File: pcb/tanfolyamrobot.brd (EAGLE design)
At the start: 81.3 x 58.7 mm, 85 parts, among them IC1 STM32F10XRXT6, IC2 7805, IC4 FT232RL, IC5 LD117AS33TR, M1 DRV8833, Q1 AO4407A, Q2 BSS123, Q3 BSS123, Q4 BSS123, X1 CSTCE08M, X2 PWR

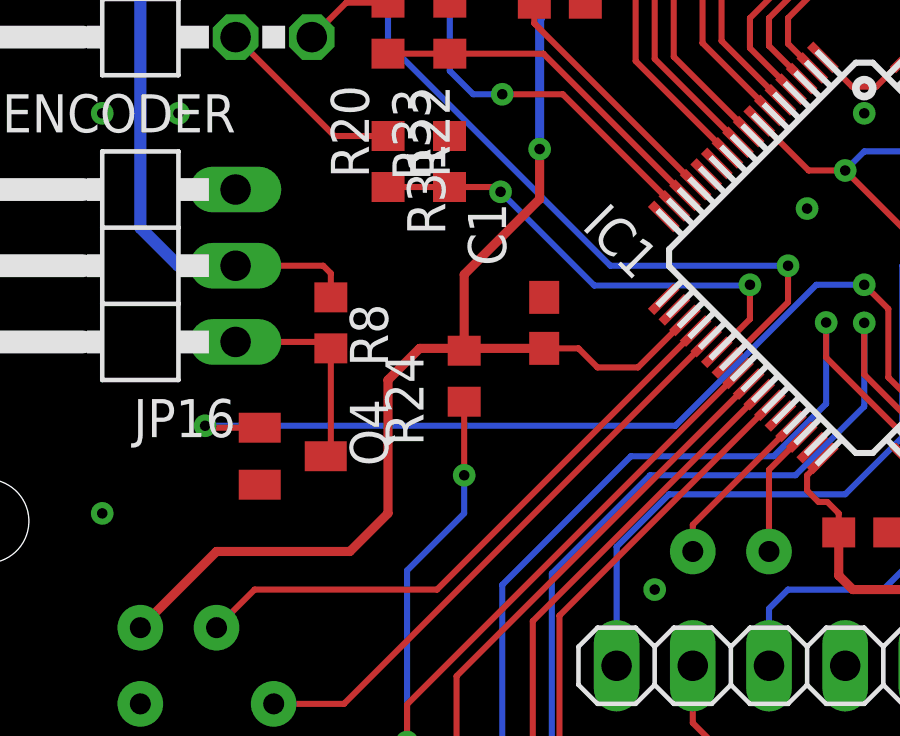
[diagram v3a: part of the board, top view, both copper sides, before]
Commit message: removed motor_faultn pullup (#1)
it can be pulled up in stm
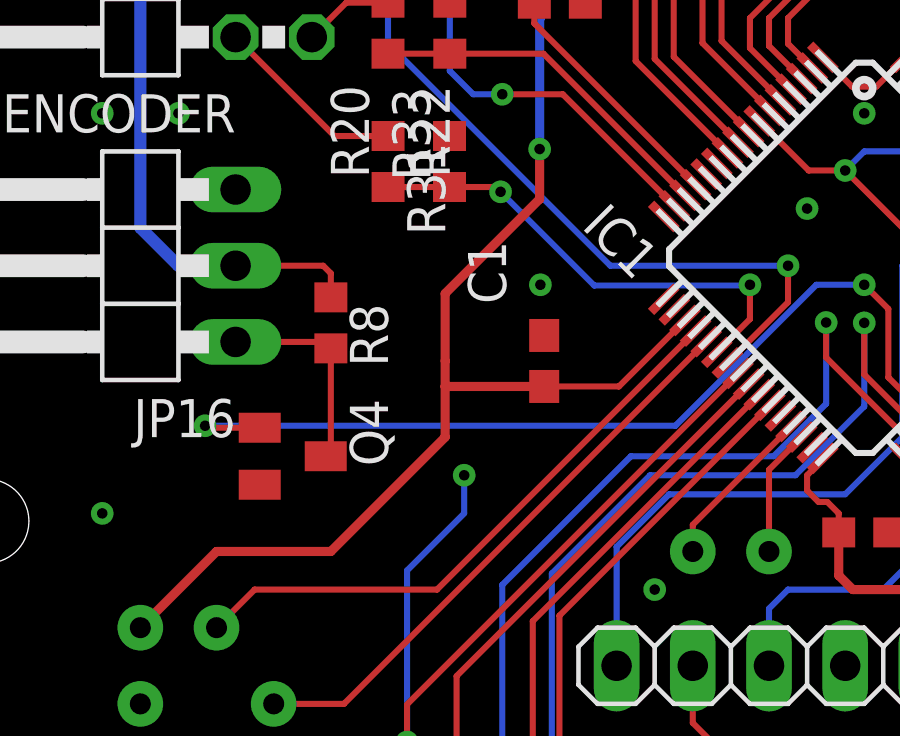
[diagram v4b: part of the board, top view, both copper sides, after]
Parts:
- removed R24: 4K7, rcl:R0603
- moved C1 1.27 mm to (21.7, 29.8)
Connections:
- net +3V3: no longer R24.1
- net MOTOR_FAULTN: no longer R24.2
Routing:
- net MOTOR_FAULTN: track 46.3 -> 43.8 mm
- net +3V3: track 241.4 -> 240.7 mm
- net GND: vias 53 -> 54
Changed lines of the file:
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@@
 <grid distance="25" unitdist="mil" unit="mil" style="dots" multiple="1" display="yes" altdistance="6.125" altunitdist="mil" altunit="mil"/>
 <layers>
-<layer number="1" name="Top" color="4" fill="1" visible="no" active="yes"/>
+<layer number="1" name="Top" color="4" fill="1" visible="yes" active="yes"/>
 <layer number="2" name="Route2" color="16" fill="1" visible="no" active="no"/>
 <layer number="3" name="Route3" color="17" fill="1" visible="no" active="no"/>
@@
 <layer number="19" name="Unrouted" color="6" fill="1" visible="yes" active="yes"/>
 <layer number="20" name="Dimension" color="24" fill="1" visible="yes" active="yes"/>
-<layer number="21" name="tPlace" color="7" fill="1" visible="no" active="yes"/>
-<layer number="22" name="bPlace" color="7" fill="1" visible="no" active="yes"/>
-<layer number="23" name="tOrigins" color="13" fill="1" visible="no" active="yes"/>
-<layer number="24" name="bOrigins" color="13" fill="1" visible="no" active="yes"/>
+<layer number="21" name="tPlace" color="7" fill="1" visible="yes" active="yes"/>
+<layer number="22" name="bPlace" color="7" fill="1" visible="yes" active="yes"/>
+<layer number="23" name="tOrigins" color="13" fill="1" visible="yes" active="yes"/>
+<layer number="24" name="bOrigins" color="13" fill="1" visible="yes" active="yes"/>
 <layer number="25" name="tNames" color="7" fill="1" visible="no" active="yes"/>
 <layer number="26" name="bNames" color="7" fill="1" visible="no" active="yes"/>
@@
 <layer number="37" name="tTest" color="7" fill="1" visible="no" active="yes"/>
 <layer number="38" name="bTest" color="7" fill="1" visible="no" active="yes"/>
-<layer number="39" name="tKeepout" color="4" fill="11" visible="no" active="yes"/>
-<layer number="40" name="bKeepout" color="1" fill="11" visible="no" active="yes"/>
-<layer number="41" name="tRestrict" color="4" fill="10" visible="no" active="yes"/>
-<layer number="42" name="bRestrict" color="1" fill="10" visible="no" active="yes"/>
+<layer number="39" name="tKeepout" color="4" fill="11" visible="yes" active="yes"/>
+<layer number="40" name="bKeepout" color="1" fill="11" visible="yes" active="yes"/>
+<layer number="41" name="tRestrict" color="4" fill="10" visible="yes" active="yes"/>
+<layer number="42" name="bRestrict" color="1" fill="10" visible="yes" active="yes"/>
 <layer number="43" name="vRestrict" color="2" fill="10" visible="no" active="yes"/>
 <layer number="44" name="Drills" color="7" fill="1" visible="no" active="yes"/>
@@
 <layer number="49" name="Reference" color="7" fill="1" visible="no" active="yes"/>
 <layer number="50" name="dxf" color="7" fill="1" visible="no" active="no"/>
-<layer number="51" name="tDocu" color="7" fill="1" visible="no" active="yes"/>
-<layer number="52" name="bDocu" color="7" fill="1" visible="no" active="yes"/>
+<layer number="51" name="tDocu" color="7" fill="1" visible="yes" active="yes"/>
+<layer number="52" name="bDocu" color="7" fill="1" visible="yes" active="yes"/>
 <layer number="53" name="tGND_GNDA" color="7" fill="9" visible="no" active="no"/>
 <layer number="54" name="bGND_GNDA" color="1" fill="9" visible="no" active="no"/>
@@
 <attribute name="VALUE" x="28.259665625" y="34.90505625" size="1.778" layer="27" rot="R315"/>
 </element>
-<element name="C1" library="rcl" library_urn="urn:adsk.eagle:library:334" package="C0603" package3d_urn="urn:adsk.eagle:package:23616/2" value="100n" x="21.717" y="31.115" smashed="yes" rot="R90">
-<attribute name="NAME" x="20.447" y="33.02" size="1.27" layer="25" rot="R90"/>
-<attribute name="POPULARITY" value="73" x="21.717" y="31.115" size="1.778" layer="27" rot="R90" display="off"/>
-<attribute name="SPICEPREFIX" value="C" x="21.717" y="31.115" size="1.778" layer="27" rot="R90" display="off"/>
-<attribute name="VALUE" x="23.622" y="30.48" size="1.27" layer="27" rot="R90"/>
+<element name="C1" library="rcl" library_urn="urn:adsk.eagle:library:334" package="C0603" package3d_urn="urn:adsk.eagle:package:23616/2" value="100n" x="21.717" y="29.845" smashed="yes" rot="R90">
+<attribute name="NAME" x="20.447" y="31.75" size="1.27" layer="25" rot="R90"/>
+<attribute name="POPULARITY" value="73" x="21.717" y="29.845" size="1.778" layer="27" rot="R90" display="off"/>
+<attribute name="SPICEPREFIX" value="C" x="21.717" y="29.845" size="1.778" layer="27" rot="R90" display="off"/>
+<attribute name="VALUE" x="23.622" y="29.21" size="1.27" layer="27" rot="R90"/>
 </element>
 <element name="C2" library="rcl" library_urn="urn:adsk.eagle:library:334" package="C0603" package3d_urn="urn:adsk.eagle:package:23616/2" value="100n" x="32.385" y="24.13" smashed="yes">
@@
 <attribute name="SPICEPREFIX" value="R" x="18.570575" y="49.82845" size="1.778" layer="27" rot="R90" display="off"/>
 <attribute name="VALUE" x="20.475575" y="49.19345" size="1.27" layer="27" rot="R90"/>
-</element>
-<element name="R24" library="rcl" library_urn="urn:adsk.eagle:library:334" package="R0603" package3d_urn="urn:adsk.eagle:package:23555/3" value="4K7" x="19.05" y="29.337" smashed="yes" rot="R270">
-<attribute name="NAME" x="16.423534375" y="30.10339375" size="1.27" layer="25" rot="R270"/>
-<attribute name="POPULARITY" value="70" x="19.05" y="29.337" size="1.778" layer="27" rot="R270" display="off"/>
-<attribute name="SPICEPREFIX" value="R" x="19.05" y="29.337" size="1.778" layer="27" rot="R270" display="off"/>
-<attribute name="VALUE" x="17.145" y="29.972" size="1.27" layer="27" rot="R270"/>
 </element>
 <element name="R25" library="rcl" library_urn="urn:adsk.eagle:library:334" package="R0603" package3d_urn="urn:adsk.eagle:package:23555/3" value="4K7" x="18.796" y="12.065" smashed="yes" rot="R90">
@@
 <contactref element="R34" pad="2"/>
 <contactref element="R33" pad="2"/>
+<via x="21.59" y="32.385" extent="1-16" drill="0.35"/>
 </signal>
 <signal name="+3V3">
@@
 <wire x1="31.006140625" y1="39.96518125" x2="31.982321875" y2="38.989" width="0.2032" layer="1"/>
 <wire x1="32.787675" y1="38.989" x2="33.76385625" y2="39.96518125" width="0.2032" layer="1"/>
-<wire x1="26.409946875" y1="31.197059375" x2="24.8428875" y2="29.63" width="0.2032" layer="1"/>
-<wire x1="24.8428875" y1="29.63" x2="23.495" y2="29.63" width="0.2032" layer="1"/>
-<wire x1="21.717" y1="30.265" x2="22.86" y2="30.265" width="0.2032" layer="1"/>
-<wire x1="23.495" y1="29.63" x2="22.86" y2="30.265" width="0.2032" layer="1"/>
-<contactref element="R24" pad="1"/>
+<wire x1="26.409946875" y1="31.197059375" x2="24.2078875" y2="28.995" width="0.2032" layer="1"/>
+<wire x1="21.717" y1="28.995" x2="24.2078875" y2="28.995" width="0.2032" layer="1"/>
 <contactref element="R29" pad="1"/>
 <via x="52.705" y="43.18" extent="1-16" drill="0.35"/>
@@
 <wire x1="21.5646" y1="41.2496" x2="21.5646" y2="36.909375" width="0.3048" layer="16"/>
 <wire x1="8.255" y1="20.955" x2="10.795" y2="23.495" width="0.3048" layer="1"/>
-<wire x1="15.24" y1="23.495" x2="16.51" y2="24.765" width="0.3048" layer="1"/>
-<wire x1="10.795" y1="23.495" x2="15.24" y2="23.495" width="0.3048" layer="1"/>
-<wire x1="16.51" y1="29.21" x2="17.565" y2="30.265" width="0.3048" layer="1"/>
-<wire x1="16.51" y1="29.21" x2="16.51" y2="24.765" width="0.3048" layer="1"/>
-<wire x1="21.717" y1="30.265" x2="19.05" y2="30.265" width="0.3048" layer="1"/>
-<wire x1="19.05" y1="30.265" x2="19.05" y2="30.187" width="0.3048" layer="1"/>
-<wire x1="17.565" y1="30.265" x2="19.05" y2="30.265" width="0.3048" layer="1"/>
-<wire x1="19.05" y1="30.187" x2="19.05" y2="32.727" width="0.3048" layer="1"/>
-<wire x1="21.5646" y1="35.2416" x2="19.05" y2="32.727" width="0.3048" layer="1"/>
+<wire x1="10.795" y1="23.495" x2="14.605" y2="23.495" width="0.3048" layer="1"/>
 <wire x1="21.5646" y1="36.909375" x2="21.5646" y2="35.2416" width="0.3048" layer="1"/>
 <wire x1="21.59" y1="43.815" x2="21.59" y2="41.275" width="0.3048" layer="16"/>
@@
 <wire x1="21.3877" y1="41.098340625" x2="26.7635" y2="35.722540625" width="0.2032" layer="1"/>
 <wire x1="31.982321875" y1="38.989" x2="32.787675" y2="38.989" width="0.2032" layer="1"/>
+<wire x1="21.5646" y1="35.2416" x2="18.415" y2="32.092" width="0.3048" layer="1"/>
+<wire x1="18.415" y1="32.092" x2="18.415" y2="29.845" width="0.3048" layer="1"/>
+<wire x1="18.415" y1="28.995" x2="18.415" y2="27.305" width="0.3048" layer="1"/>
+<wire x1="18.415" y1="27.305" x2="14.605" y2="23.495" width="0.3048" layer="1"/>
+<wire x1="21.717" y1="28.995" x2="18.415" y2="28.995" width="0.3048" layer="1"/>
+<wire x1="18.415" y1="28.995" x2="18.415" y2="29.845" width="0.3048" layer="1"/>
 </signal>
 <signal name="SWD_SWO">
@@
 <signal name="MOTOR_FAULTN">
 <contactref element="M1" pad="!FAULT"/>
-<contactref element="R24" pad="2"/>
 <wire x1="13.335" y1="2.54" x2="15.24" y2="2.54" width="0.2032" layer="1"/>
 <contactref element="IC1" pad="24"/>
@@
 <wire x1="17.145" y1="18.396578125" x2="17.145" y2="17.145" width="0.2032" layer="1"/>
 <wire x1="17.145" y1="17.145" x2="17.145" y2="4.445" width="0.2032" layer="1"/>
-<wire x1="19.05" y1="28.487" x2="19.05" y2="26.035" width="0.2032" layer="1"/>
 <via x="19.05" y="26.035" extent="1-16" drill="0.35"/>
 <wire x1="19.05" y1="26.035" x2="19.05" y2="24.765" width="0.2032" layer="16"/>

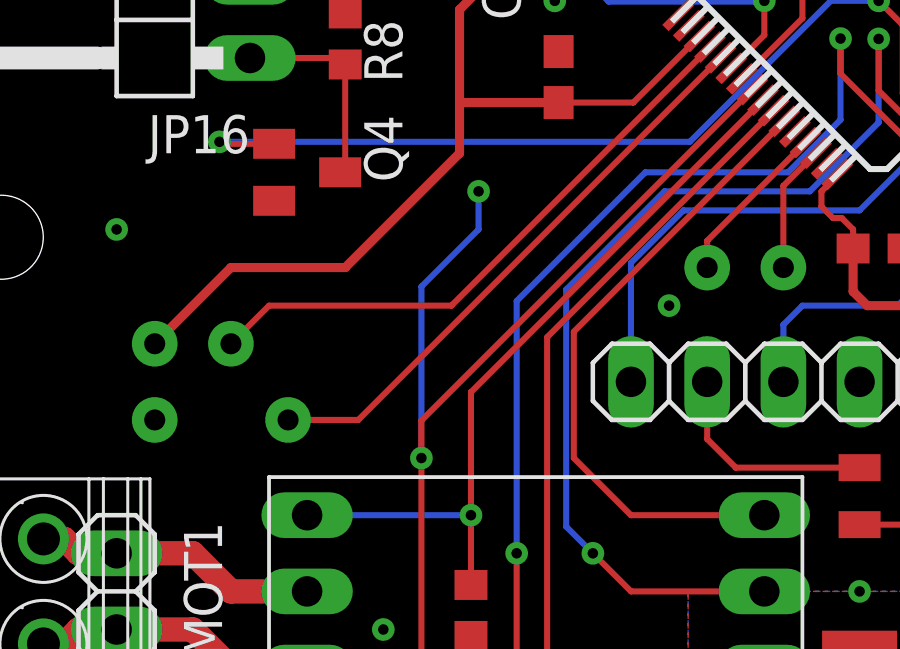
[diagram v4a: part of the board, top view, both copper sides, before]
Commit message: removed motor_faultn pullup's wire stub (#1)
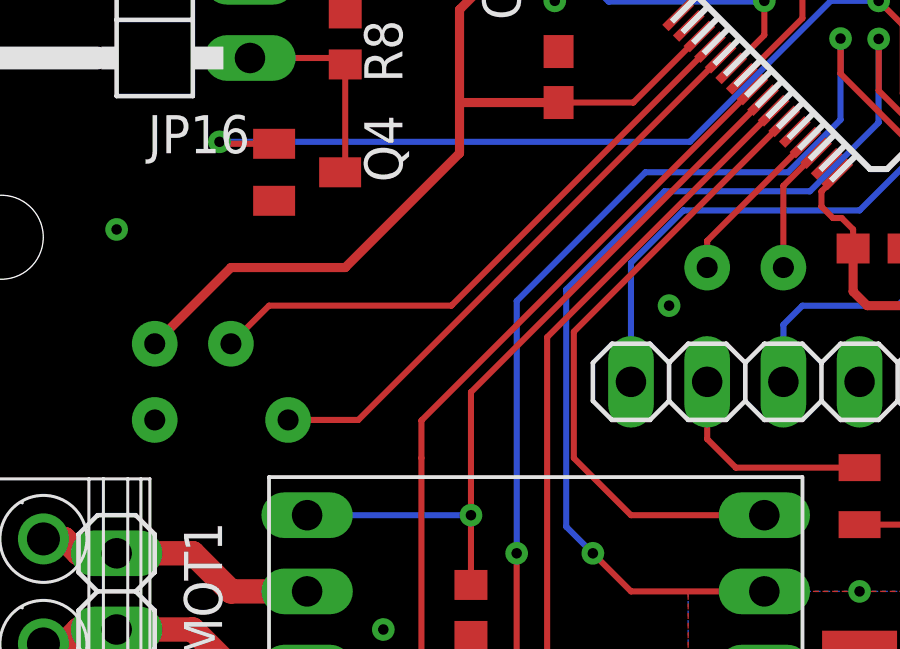
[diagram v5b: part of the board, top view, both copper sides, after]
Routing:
- net MOTOR_FAULTN: track 43.8 -> 34.2 mm, vias 2 -> 0
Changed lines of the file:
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@@
 <wire x1="17.145" y1="18.396578125" x2="17.145" y2="17.145" width="0.2032" layer="1"/>
 <wire x1="17.145" y1="17.145" x2="17.145" y2="4.445" width="0.2032" layer="1"/>
-<via x="19.05" y="26.035" extent="1-16" drill="0.35"/>
-<wire x1="19.05" y1="26.035" x2="19.05" y2="24.765" width="0.2032" layer="16"/>
-<wire x1="19.05" y1="24.765" x2="17.145" y2="22.86" width="0.2032" layer="16"/>
-<wire x1="17.145" y1="22.86" x2="17.145" y2="17.145" width="0.2032" layer="16"/>
-<via x="17.145" y="17.145" extent="1-16" drill="0.35"/>
 </signal>
 <signal name="MOTOR1_IN1">
